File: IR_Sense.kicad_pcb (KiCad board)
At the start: 2 copper layers, 354.9 x 338.6 mm, 12 parts, among them J1 Conn_01x04, J2 Conn_01x02, Q1 SFH320, U2 LMV321

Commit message: change IR diode and photo transistor
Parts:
- removed the G*** at (188.6, 37.6)
- added G***: LOGO, LOGO, B.Cu at (85.0, 75.1)
- added G***: LOGO, LOGO, B.Cu at (102.6, 74.8)
- added H1: MountingHole_Pad, MountingHole:MountingHole_2.2mm_M2_DIN965_Pad, F.Cu at (98.8, 68.2)
- added H2: MountingHole_Pad, MountingHole:MountingHole_2.2mm_M2_DIN965_Pad, F.Cu at (89.8, 68.2)
- added H3: MountingHole_Pad, MountingHole:MountingHole_2.2mm_M2_DIN965_Pad, F.Cu at (81.8, 81.9)
- added H4: MountingHole_Pad, MountingHole:MountingHole_2.2mm_M2_DIN965_Pad, F.Cu at (106.8, 81.9)
- D1: value IR26-21C_L110_TR8 -> VSMY2850G; footprint LED_SMD:LED_1206_3216Metric -> IR_Sense:VSMY2850G_VEMT2020X01
- J1: value Conn_01x04 -> Conn_01x03
- Q1: value SFH320 -> Q_Photo_NPN_EC; footprint LED_SMD:LED_PLCC-2_3.4x3.0mm_KA -> IR_Sense:VSMY2850G_VEMT2020X01
- R3: value 10k -> 5k
- moved Q1 97.7 mm to (100.1, 73.0), turned to -90 degrees
- moved R8 97.5 mm to (102.1, 69.2), turned to -90 degrees
- moved R3 95.1 mm to (106.2, 71.6), turned to 135 degrees
- moved R5 94.9 mm to (103.7, 70.1), turned to -90 degrees
- moved J2 94.2 mm to (83.0, 75.7)
- moved R7 94.1 mm to (101.2, 77.7), turned to -90 degrees
- moved D1 93.4 mm to (88.5, 73.0), turned to 50 degrees
- moved U2 92.9 mm to (103.6, 73.9), turned to -90 degrees
- moved R6 91.3 mm to (103.6, 76.7), turned to 180 degrees
- moved R1 90.8 mm to (83.9, 71.6), turned to 180 degrees
- moved J1 85.9 mm to (107.2, 76.5), turned to 90 degrees
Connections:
- J1 pad 2: IR I/O -> GND
- J1 pad 3: GND_Sense -> IR I/O
- Q1 pad 1: +3.3V -> GND
- Q1 pad 2: Net-(Q1-E) -> Net-(Q1-C)
- R3 pad 1: Net-(Q1-E) -> +3.3V
- R3 pad 2: GND_Sense -> Net-(Q1-C)
- R5 pad 1: Net-(Q1-E) -> Net-(Q1-C)
- R8 pad 1: GND_Sense -> GND
- U2 pad 2: GND_Sense -> GND
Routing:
- net GND_Sense: track 10.0 -> 0.00 mm, vias 3 -> 0
- net Net-(Q1-E): track 8.47 -> 0.00 mm
- net Net-(Q1-C): track 0.00 -> 7.59 mm
- net GND: track 7.83 -> 3.38 mm, vias 0 -> 3
- net Net-(D1-K): track 8.97 -> 4.99 mm
- net +3.3V: track 16.2 -> 12.4 mm, vias 2 -> 3
- net Net-(R7-Pad1): track 9.63 -> 7.72 mm
- net +5V: track 3.78 -> 5.00 mm
- net Net-(R5-Pad2): track 6.56 -> 7.63 mm
- net IR I/O: track 6.76 -> 7.30 mm
- added copper zone on B.Cu, net GND
- removed copper zone on B.Cu, net GND_Sense
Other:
- board size 354.9 x 338.6 mm -> 29.6 x 18.2 mm
- board text added: "+"
- board text added: "+-D"
- board text added: "-"
- board text added: "3V3"
- board text added: "IRIO"
- board text added: "JLCJLCJLCJLCJLC"
- board text added: "Martin.L"
- board text added: "SSL26"
- board text removed: "2.7k"
- board text removed: "3.3V"
- board text removed: "3k"
- board text removed: "5.6k"
- board text removed: "5k"
- board text removed: "66k"
- board text removed: "IR I/O"
- board text removed: "LMV321"
- board text removed: "RX"
- board text removed: "TX"

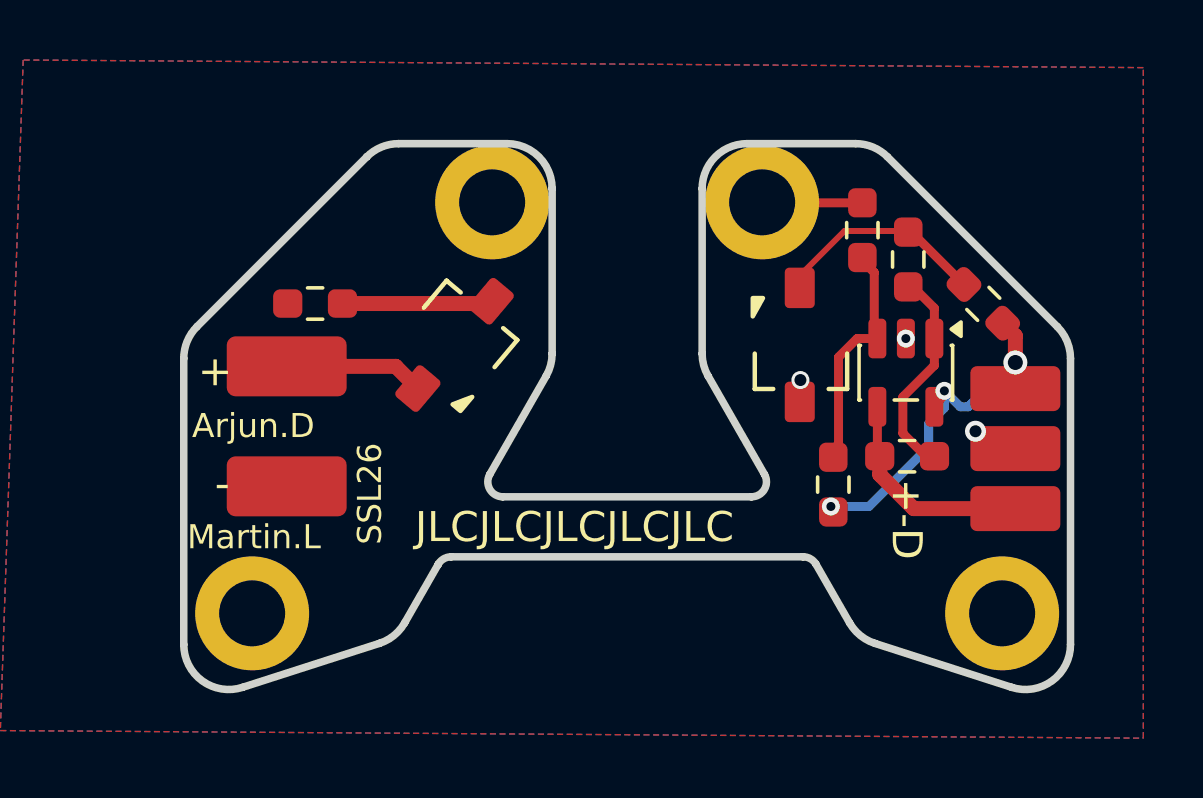
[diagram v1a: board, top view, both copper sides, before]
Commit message: reduced board size update
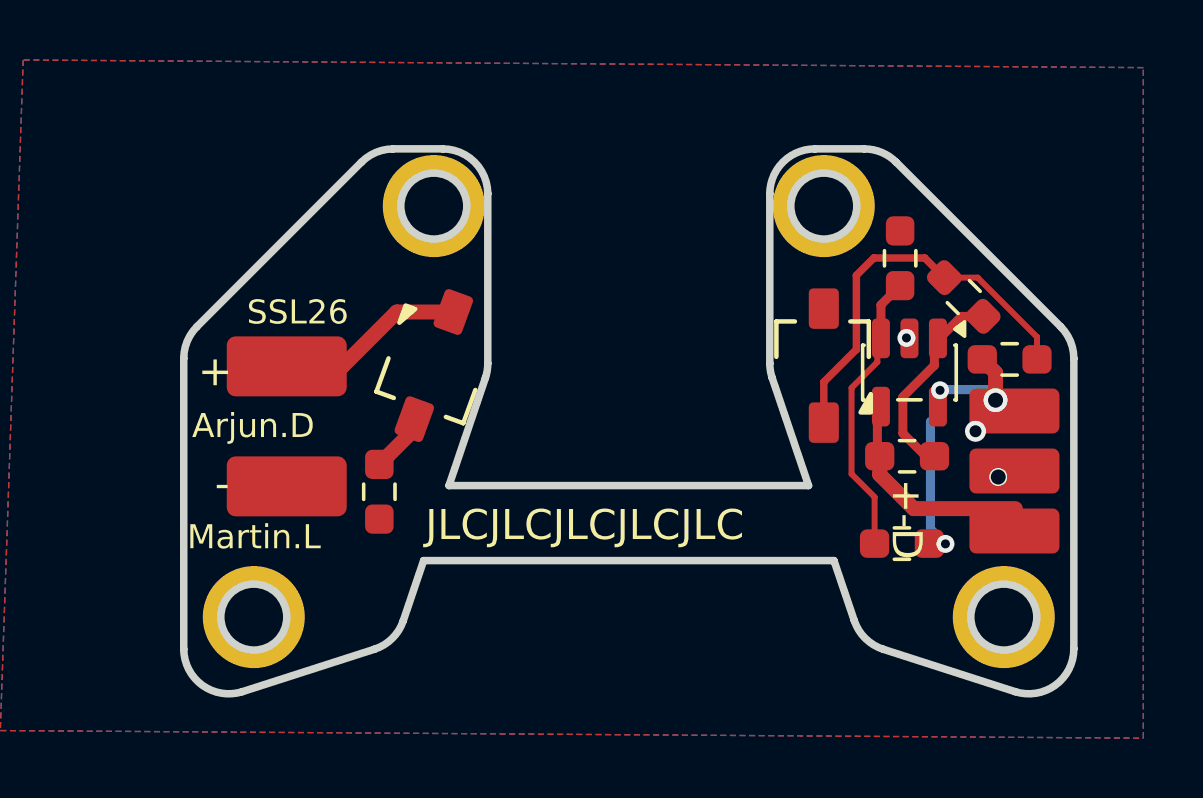
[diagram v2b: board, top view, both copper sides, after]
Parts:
- Q1: value Q_Photo_NPN_EC -> VEMT2020X01
- moved H4 24.9 mm to (81.9, 82.1)
- moved H3 23.4 mm to (100.9, 68.4)
- moved H1 16.0 mm to (106.9, 82.1)
- moved R1 6.63 mm to (86.0, 77.9), turned to -90 degrees
- moved R7 3.02 mm to (103.5, 79.6), turned to 0 degrees
- moved R5 2.23 mm to (105.5, 71.4), turned to -45 degrees
- moved R3 2.05 mm to (107.0, 73.5), turned to 0 degrees
- moved H2 1.95 mm to (87.9, 68.4)
- moved G*** 1.68 mm to (104.2, 75.2), turned to 110 degrees
- moved R8 1.57 mm to (103.4, 70.1)
- moved Q1 1.06 mm to (100.9, 73.7), turned to 90 degrees
- moved D1 0.98 mm to (87.9, 73.7), turned to -110 degrees
- moved G*** 0.84 mm to (84.2, 75.3)
- moved J1 0.75 mm to (107.2, 77.2)
- moved U2 0.12 mm to (103.7, 73.9)
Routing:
- net Net-(Q1-C): track 7.59 -> 13.5 mm
- net GND: track 3.38 -> 0.01 mm, vias 3 -> 2
- net Net-(D1-K): track 4.99 -> 1.99 mm
- net +3.3V: track 12.4 -> 10.1 mm, vias 3 -> 4
- net Net-(R7-Pad1): track 7.72 -> 9.42 mm
- net +5V: track 5.00 -> 6.30 mm
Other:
- board size 29.6 x 18.2 mm -> 29.7 x 18.2 mm
